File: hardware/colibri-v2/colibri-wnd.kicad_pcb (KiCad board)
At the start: 4 copper layers, 120 x 110 mm, 528 parts, among them CN1 XT60-M, CN10 629_105_150_921, CN11 629_105_150_921, CN12 XT60-F, CN2 XT60-F, CN3 AS0B821-S78B-7H, CN4 HDMI_A, CN5 692_121_030_100, CN6 Wurth-68715014522-LCD, CN7 MOLEX_73366_0061, CN8 629_105_150_921, CN9 Wurth-68711814522, CON1 PJ-102AH, P1 CONN_02X10, P10 CONN_01X08, P11 CONN_01X03, P12 CONN_01X03, P13 CONN_01X03, P14 CONN_01X03, P15 CONN_01X03, P16 CONN_01X03, P17 CONN_01X03, P18 CONN_01X03, P19 CONN_01X03, P20 CONN_01X03, P21 CONN_01X03, P22 CONN_01X03, P23 CONN_01X03, P24 CONN_01X03, P25 CONN_01X03, P26 CONN_01X03, P27 CONN_01X03, P28 CONN_01X03, P29 CONN_01X03, P3 CONN_02X01, P30 CONN_01X03, P31 CONN_01X03, P32 CONN_02X10, P33 ECM00870-L, P34 ECM00870-L, P35 STANDOFF, P36 STANDOFF, P37 STANDOFF, P38 STANDOFF, P39 STANDOFF, P4 ECM00870-L, P40 STANDOFF, P5 ECM00870-L, P6 CONN_01X08, P7 CONN_01X04, P8 CONN_01X04, P9 CONN_01X04, Q10 PDTC123JU, Q11 PDTA123JU, Q12 IRLML6402TRPBF, Q13 BSS138PW, Q14 PDTA123JU, Q15 BSS138PW, Q16 BSS138PW, Q17 IRLML6402TRPBF, Q3 BSS138PW, Q4 FDMA530PZ, Q5 BSS138PW, Q6 BSS138PW, Q7 BSS138PW, Q8 AP6681GMT-HF-3TR, Q9 FDMA530PZ, SW1 OMRON B3F-1070, SW10 OMRON B3F-1070, SW11 OMRON B3F-1070, SW2 OMRON B3F-1070, SW3 OMRON B3F-1070, SW4 OMRON B3F-1070, SW5 OMRON B3F-1070, SW6 OMRON B3F-1070, SW7 OMRON B3F-1070, SW8 OMRON B3F-1070, SW9 ALPS-SPPJ320600, U1 L3GD20HTR, U10 TPS2065CDBVT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

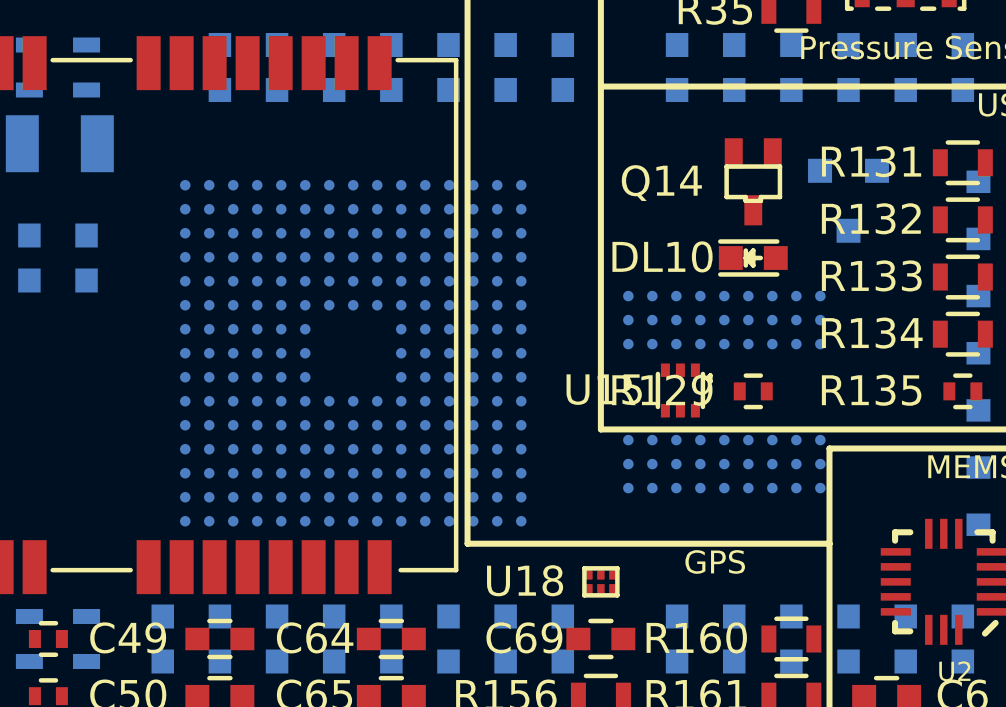
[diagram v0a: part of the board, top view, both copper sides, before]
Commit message: Added lib.pretty/tfbga-216-32.kicad_mod  lib.pretty/tfbga-54-32.kicad_mod
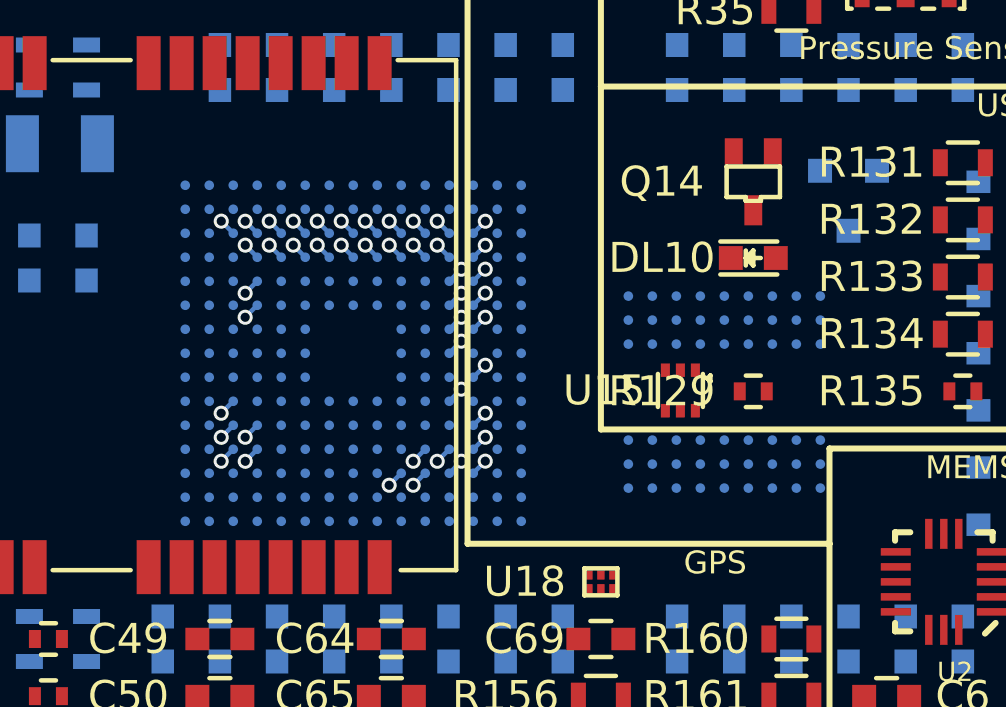
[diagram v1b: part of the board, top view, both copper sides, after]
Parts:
- U25: footprint Sigmadrone:tfbga-216-35 -> Sigmadrone:tfbga-216-32
- U3: footprint Sigmadrone:tfbga-54-35 -> Sigmadrone:tfbga-54-32
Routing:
- net /cortex/IN_PWM_03: track 0.00 -> 0.57 mm, vias 0 -> 1
- net /Leds/Buttons/BUTTON_2: track 0.00 -> 0.57 mm, vias 0 -> 1
- net /STM32F4 SDRAM/FMC_D3: track 0.00 -> 0.57 mm, vias 0 -> 1
- net /STM32F4 SDRAM/FMC_D0: track 0.00 -> 0.57 mm, vias 0 -> 1
- net /STM32F4 SDRAM/FMC_A7: track 0.00 -> 0.57 mm, vias 0 -> 1
- net /cortex/PCA9685_OE: track 0.00 -> 0.57 mm, vias 0 -> 1
- net /STM32F4 SDRAM/FMC_A6: track 0.00 -> 0.57 mm, vias 0 -> 1
- net /Leds/Buttons/LED3: track 0.00 -> 0.57 mm, vias 0 -> 1
- net /Leds/Buttons/LED0: track 0.00 -> 0.57 mm, vias 0 -> 1
- net /External Sensors/C_SPI2_NSS2: track 0.00 -> 0.57 mm, vias 0 -> 1
- net /cortex/IN_PWM_04: track 0.00 -> 0.57 mm, vias 0 -> 1
- net /cortex/C_OTG_FS_PSO: track 0.00 -> 0.57 mm, vias 0 -> 1
- net /Power Control/ADAPTER_AV#: track 0.00 -> 0.57 mm, vias 0 -> 1
- net /External Sensors/C_I2C2_SCL: track 0.00 -> 0.57 mm, vias 0 -> 1
- net +3V3: track 0.00 -> 0.57 mm, vias 0 -> 1
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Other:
- copper layers 4 -> 6
- net class Default: clearance 0.1778 -> 0.1524; trace_width 0.2032 -> 0.1524; via_dia 0.889 -> 0.50292; via_drill 0.635 -> 0.3048
- net class Power: trace_width 0.254 -> 0.2032; via_dia 0.889 -> 0.635; via_drill 0.635 -> 0.381
- rule trace_clearance: 0.1778 -> 0.1524
- rule trace_min: 0.1524 -> 0.1
- rule via_min_drill: 0.3302 -> 0.25
- rule via_min_size: 0.508 -> 0.4

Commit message: Work on cortex routing
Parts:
- moved C13 68.8 mm to (32.4, 97.2)
- moved C14 68.8 mm to (32.4, 99.1)
- moved C15 68.8 mm to (32.4, 101.0)
- moved C16 68.8 mm to (32.4, 102.9)
- moved C17 68.8 mm to (32.4, 104.8)
- moved C18 68.8 mm to (32.4, 106.7)
- moved C19 68.8 mm to (32.4, 108.6)
- moved R35 62.2 mm to (61.0, 33.7)
- moved R36 62.2 mm to (61.0, 31.8)
- moved R37 62.2 mm to (61.0, 29.8)
- moved U5 62.2 mm to (64.8, 31.8)
- moved C124 62.2 mm to (73.0, 31.8)
- moved C25 62.2 mm to (73.0, 33.7)
- moved R34 62.2 mm to (73.0, 29.8)
- moved U15 59.1 mm to (87.0, 40.0)
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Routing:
- net (no net): track 0.00 -> 30.7 mm, vias 0 -> 7
- net /cortex/VCAP2: track 0.00 -> 10.3 mm, vias 0 -> 2
- net /Leds/Buttons/LED4: track 0.57 -> 10.8 mm, vias 1 -> 2
- net /cortex/PI9: track 0.57 -> 10.0 mm, vias 1 -> 2
- net /cortex/USART2_RTS: track 0.57 -> 9.85 mm, vias 1 -> 2
- net /STM32F4 SDRAM/FMC_D0: track 0.57 -> 9.48 mm, vias 1 -> 2
- net /Leds/Buttons/BOOT0: track 0.00 -> 8.48 mm, vias 0 -> 2
- net /MEMS/MEMS_ACC_INT1: track 0.57 -> 8.63 mm, vias 1 -> 2
- net /STM32F4 SDRAM/FMC_D1: track 0.57 -> 8.29 mm, vias 1 -> 2
- net /Wandboard Connector/WB_SPI_CS: track 0.00 -> 7.59 mm, vias 0 -> 2
- net /External Sensors/C_SPI2_MOSI: track 0.00 -> 7.47 mm, vias 0 -> 2
- net /cortex/PI10: track 0.57 -> 8.04 mm, vias 1 -> 2
- net /cortex/PH14: track 0.00 -> 7.43 mm, vias 0 -> 2
- net /cortex/PH15: track 0.00 -> 7.38 mm, vias 0 -> 2
- net /STM32F4 SDRAM/FMC_A5: track 0.57 -> 7.85 mm, vias 1 -> 2
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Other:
- net class Default: via_dia 0.50292 -> 0.4826

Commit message: Work on cortex routing
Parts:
- moved U3 3.86 mm to (73.7, 95.2)
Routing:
- net /STM32F4 SDRAM/FMC_SDCKE0: track 3.87 -> 14.0 mm
- net /External Sensors/C_I2C2_SCL: track 2.53 -> 11.1 mm
- net /STM32F4 SDRAM/FMC_A6: track 2.18 -> 10.6 mm
- net /STM32F4 SDRAM/FMC_SDNE0: track 4.24 -> 12.3 mm
- net /Leds/Buttons/BUTTON_2: track 3.47 -> 10.9 mm
- net /Leds/Buttons/BUTTON_0: track 3.53 -> 6.69 mm
- net /Leds/Buttons/LED3: track 7.54 -> 5.09 mm
- net (no net): track 30.7 -> 28.4 mm
- net /STM32F4 SDRAM/FMC_A5: track 7.85 -> 5.70 mm
- net /External Sensors/C_I2C2_SDA: track 7.64 -> 5.61 mm
- net /Leds/Buttons/LED2: track 7.09 -> 5.31 mm
- net /cortex/OSC-IN: track 5.23 -> 3.46 mm
- net /Leds/Buttons/LED0: track 5.93 -> 4.20 mm
- net /JTAG/SWD/RESET#: track 5.03 -> 3.45 mm
- net /cortex/PWM_SRV_EN: track 7.49 -> 5.95 mm
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
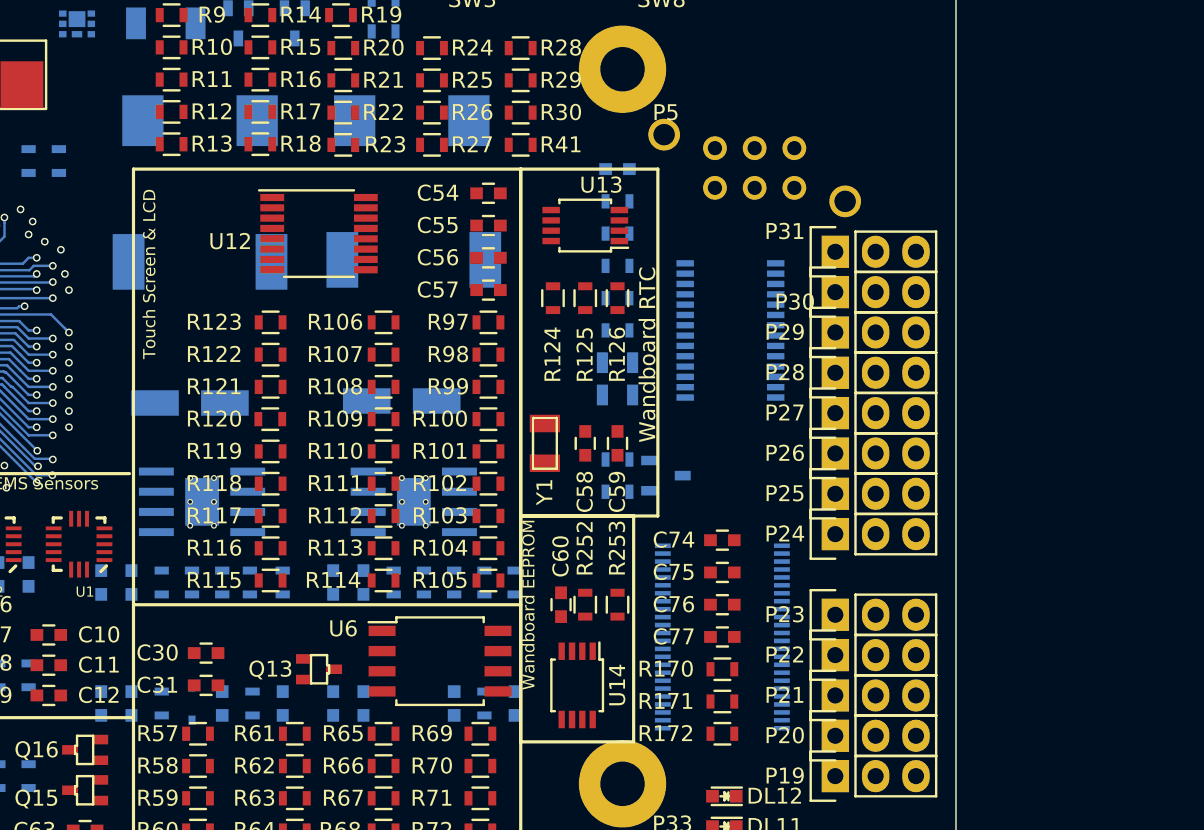
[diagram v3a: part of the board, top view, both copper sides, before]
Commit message: Rearanged Voltage regulators
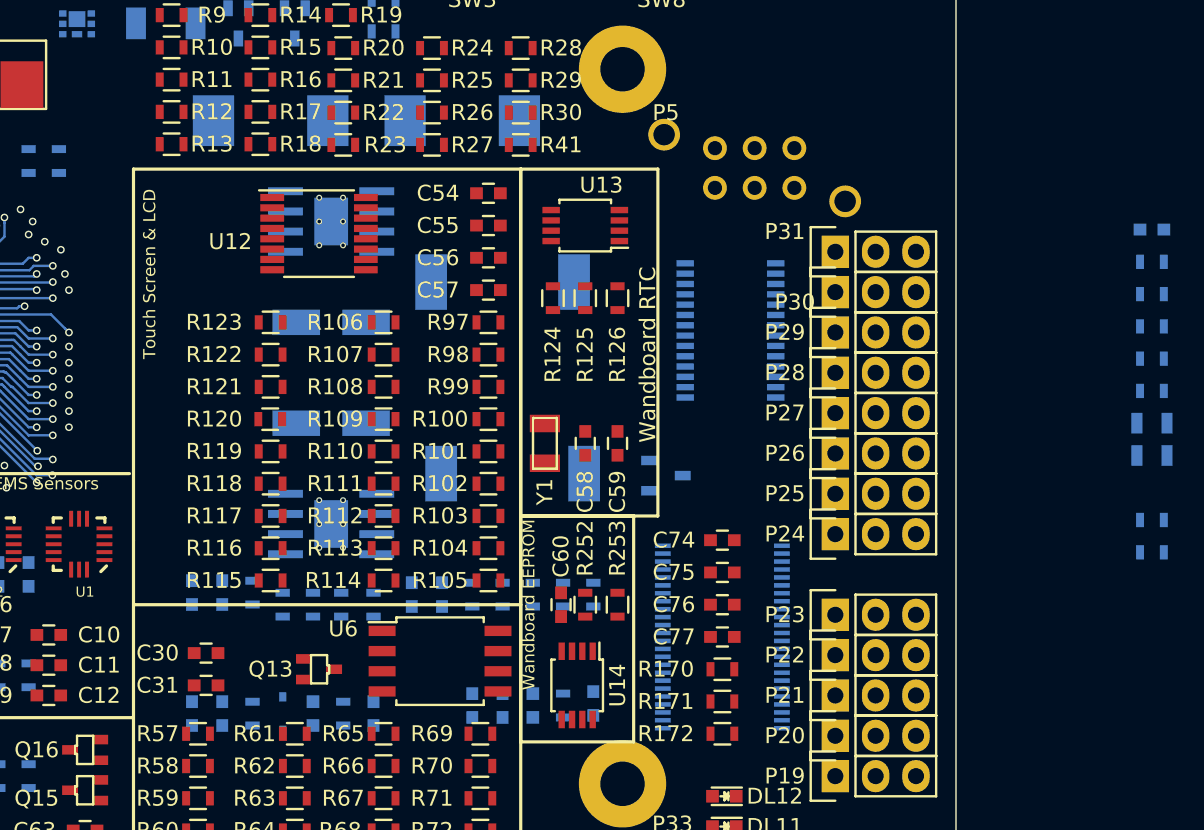
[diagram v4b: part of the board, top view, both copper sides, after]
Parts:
- moved C88 33.9 mm to (172.3, 85.6)
- moved R186 33.9 mm to (172.3, 99.8)
- moved R187 33.9 mm to (172.3, 97.8)
- moved R188 33.9 mm to (172.3, 95.8)
- moved R189 33.9 mm to (172.3, 93.7)
- moved R190 33.9 mm to (172.3, 91.7)
- moved R191 33.9 mm to (172.3, 89.7)
- moved R192 33.9 mm to (172.3, 87.6)
- moved R55 33.9 mm to (172.3, 103.9)
- moved R56 33.9 mm to (172.3, 105.9)
- moved L5 23.8 mm to (132.1, 101.0), turned to 270 degrees
- moved U22 18.4 mm to (120.7, 85.1)
- moved C122 8.98 mm to (120.7, 97.8)
- moved C84 8.76 mm to (131.4, 115.6)
- moved C86 8.76 mm to (129.5, 115.6)
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
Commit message: Work on cortex routing
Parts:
- U25: footprint Sigmadrone:tfbga-216-32 -> Sigmadrone:tfbga-216-34
- U3: footprint Sigmadrone:tfbga-54-32 -> Sigmadrone:tfbga-54-34
- moved R204 32.6 mm to (78.7, 89.5)
- moved R205 31.0 mm to (80.6, 89.5), turned to 90 degrees
- moved R206 30.5 mm to (82.5, 89.5), turned to 90 degrees
- moved R202 6.60 mm to (84.4, 120.0), turned to 90 degrees
- moved U3 4.08 mm to (71.2, 92.0)
- moved U25 0.21 mm to (93.2, 93.2)
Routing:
- net (no net): track 28.4 -> 0.00 mm, vias 7 -> 0
- net /STM32F4 SDRAM/FMC_SDCKE0: track 14.0 -> 0.00 mm, vias 2 -> 0
- net /STM32F4 SDRAM/FMC_SDNE0: track 12.3 -> 0.00 mm, vias 2 -> 0
- net /External Sensors/C_I2C2_SCL: track 11.1 -> 0.00 mm, vias 2 -> 0
- net /Leds/Buttons/BUTTON_2: track 10.9 -> 0.00 mm, vias 2 -> 0
- net /STM32F4 SDRAM/FMC_A6: track 10.6 -> 0.00 mm, vias 2 -> 0
- net /cortex/VCAP2: track 10.3 -> 0.00 mm, vias 2 -> 0
- net /Leds/Buttons/LED4: track 10.1 -> 0.00 mm, vias 2 -> 0
- net /cortex/USART2_RTS: track 9.85 -> 0.00 mm, vias 2 -> 0
- net /cortex/PI9: track 9.75 -> 0.00 mm, vias 2 -> 0
- net /STM32F4 SDRAM/FMC_D0: track 9.48 -> 0.00 mm, vias 2 -> 0
- net /Wandboard Connector/WB_SPI_CS: track 8.65 -> 0.00 mm, vias 2 -> 0
- net /MEMS/MEMS_ACC_INT1: track 8.63 -> 0.00 mm, vias 2 -> 0
- net /cortex/PI7: track 8.44 -> 0.00 mm, vias 2 -> 0
- net /STM32F4 SDRAM/FMC_D1: track 8.29 -> 0.00 mm, vias 2 -> 0
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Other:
- net class Default: clearance 0.1524 -> 0.1016; trace_width 0.1524 -> 0.127; via_drill 0.3048 -> 0.254
- rule trace_clearance: 0.1524 -> 0.1016
- rule trace_min: 0.1 -> 0.1016
- rule via_min_drill: 0.25 -> 0.2032
- rule via_min_size: 0.4 -> 0.381

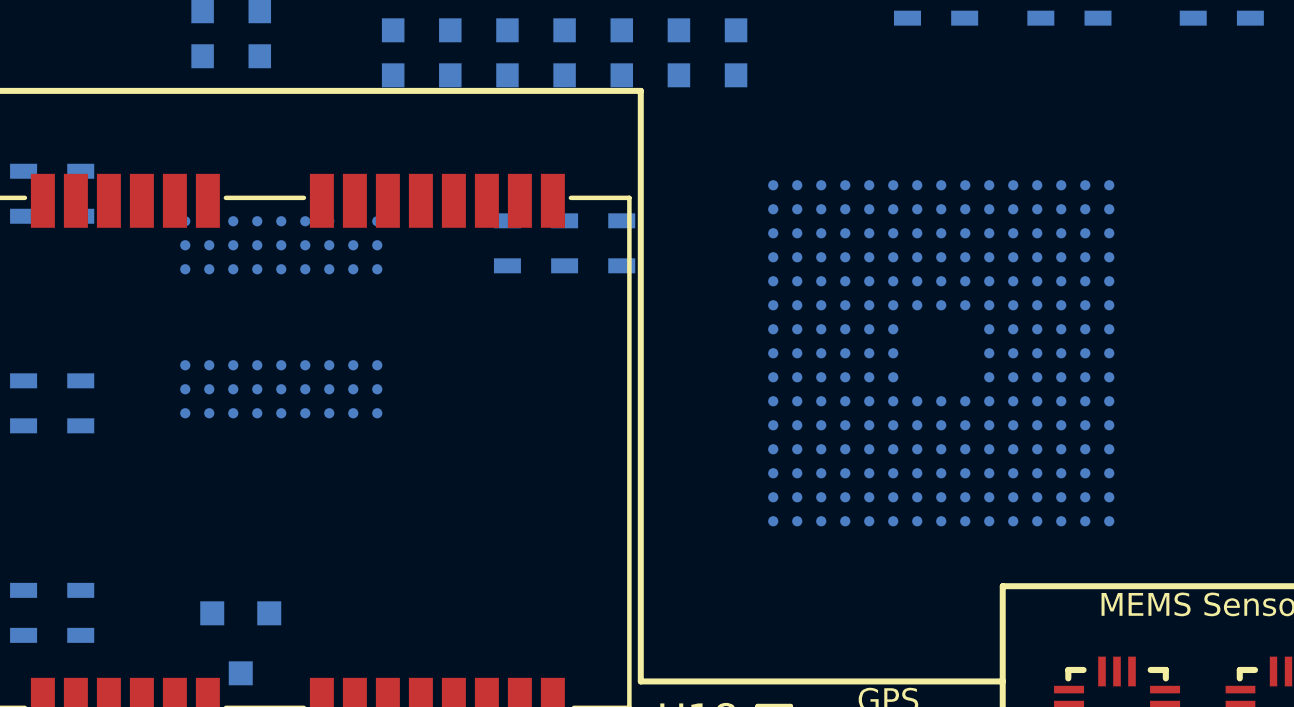
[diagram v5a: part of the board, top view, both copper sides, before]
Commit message: Reverted the TFBGA ball size back to 0.35mm
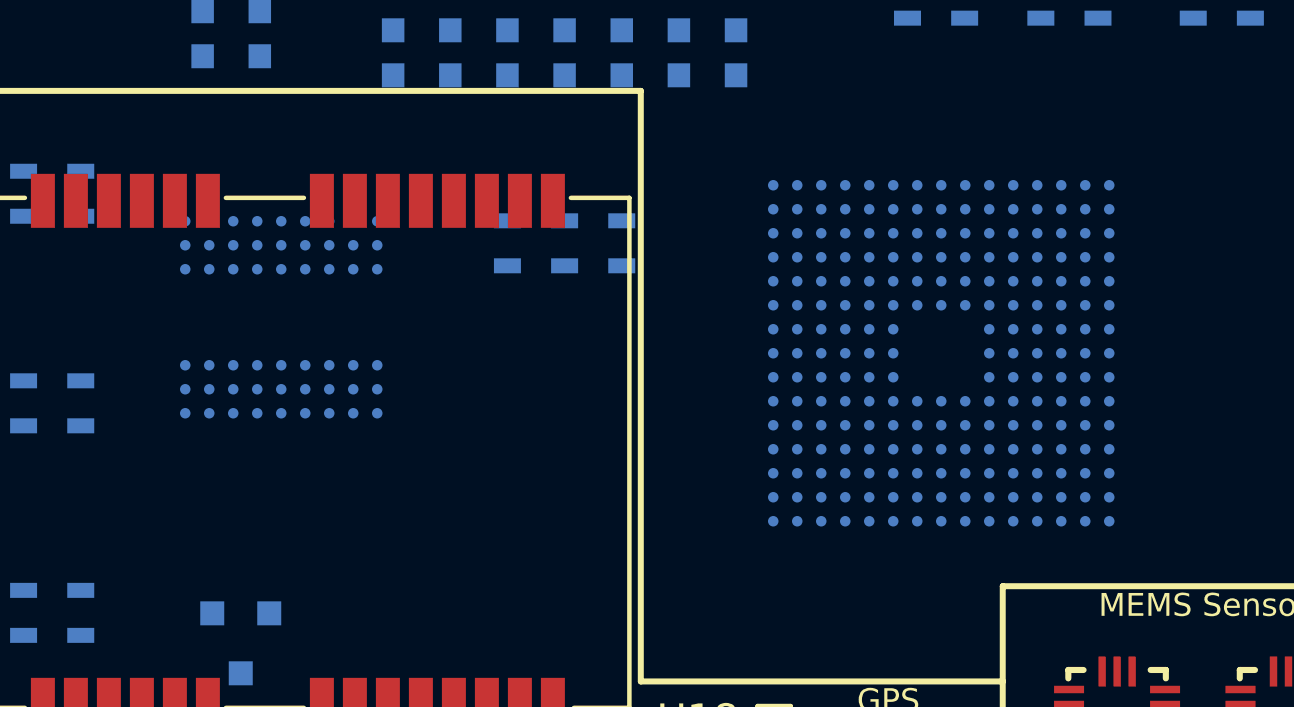
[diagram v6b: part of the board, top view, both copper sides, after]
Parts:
- U25: footprint Sigmadrone:tfbga-216-34 -> Sigmadrone:tfbga-216-35
- U3: footprint Sigmadrone:tfbga-54-34 -> Sigmadrone:tfbga-54-35
